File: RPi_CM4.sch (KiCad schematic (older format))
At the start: 12 parts, among them J1 Micro_SD_Card, U6 Compute_Module_4_Connectors

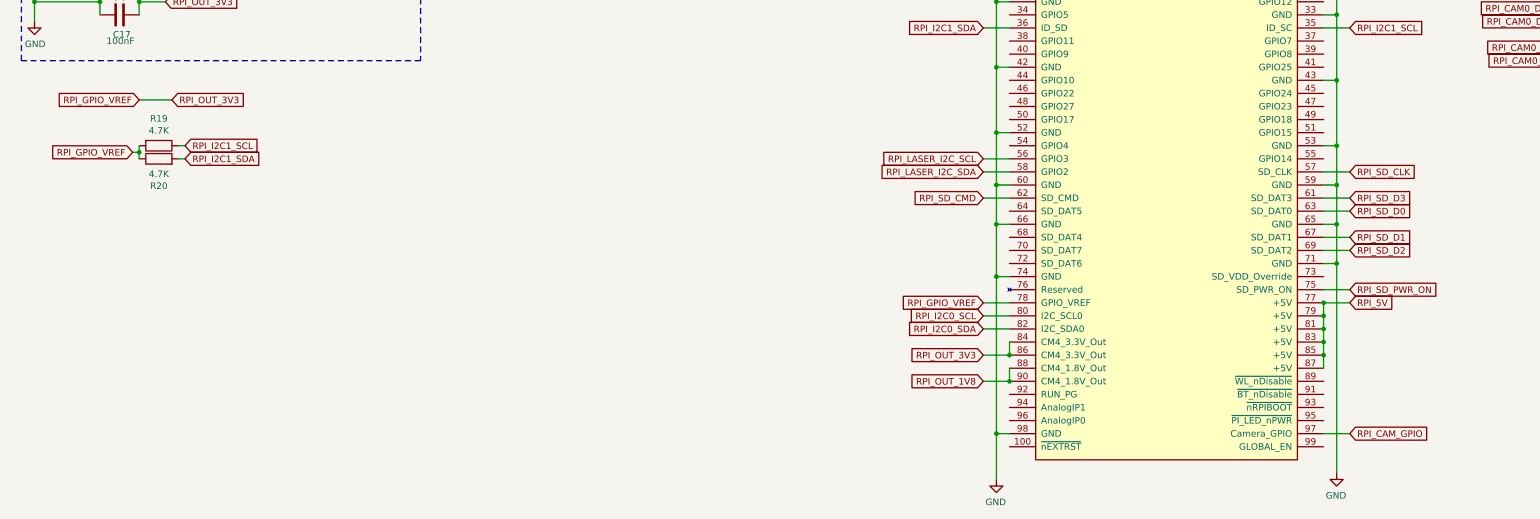
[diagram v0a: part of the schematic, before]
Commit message: start migrating to kicad v6
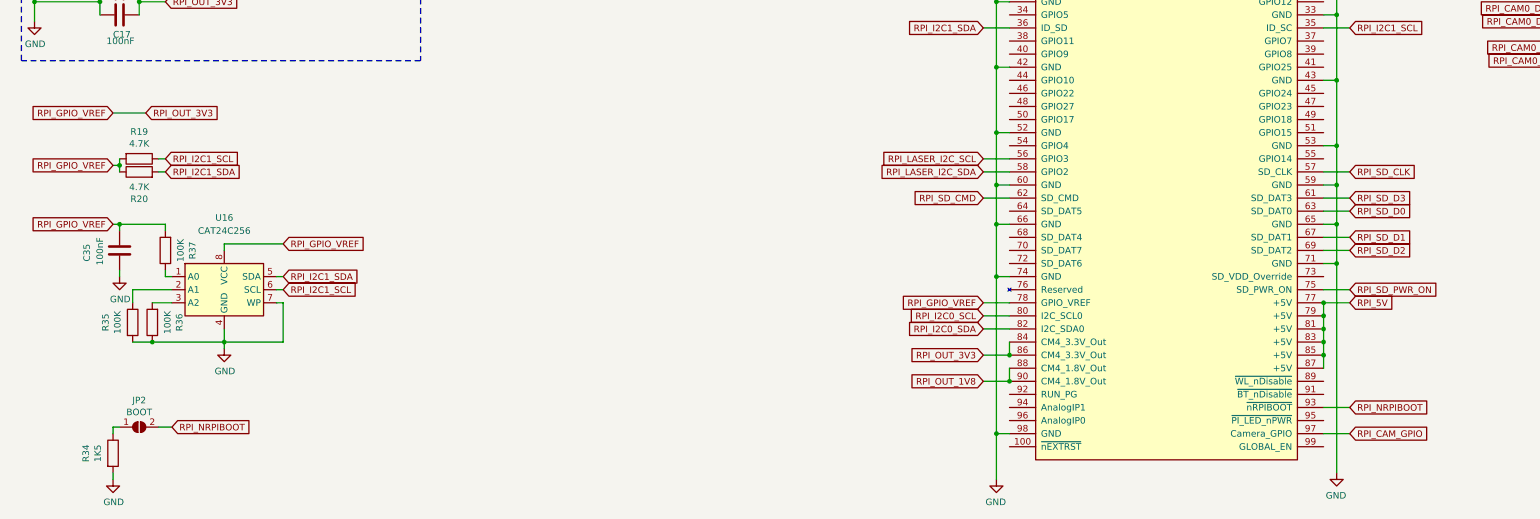
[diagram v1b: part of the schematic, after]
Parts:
- added C35: 100nF, Capacitor_SMD:C_0402_1005Metric, symbol Device:C
- added JP2: BOOT, Jumper:SolderJumper-2_P1.3mm_Open_TrianglePad1.0x1.5mm, symbol Jumper:SolderJumper_2_Open
- added R34: 1K5, Resistor_SMD:R_0402_1005Metric, symbol Device:R
- added R35, R36, R37: 100K, Resistor_SMD:R_0402_1005Metric, symbol Device:R
- added U16: CAT24C256, Package_DFN_QFN:DFN-8-1EP_3x2mm_P0.5mm_EP1.3x1.5mm, symbol Memory_EEPROM:CAT24C256
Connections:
- net GND: now also C35.1, R34.2, R35.2, R36.1, U16.4 (GND), U16.7 (WP)
- net RPI_GPIO_VREF: now also C35.2, R37.2, U16.8 (VCC)
- net RPI_I2C1_SCL: now also U16.6 (SCL)
- net RPI_I2C1_SDA: now also U16.5 (SDA)
- net RPI_NRPIBOOT: now reaches U6.93 (~nRPIBOOT)
- net RPI_NRPIBOOT: now also JP2.2 (B)
- new net: R37.1, U16.1 (A0)
- new net: R35.1, U16.2 (A1)
- new net: R36.2, U16.3 (A2)
- new net: JP2.1 (A), R34.1
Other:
- moved on the sheet: R19, R20
